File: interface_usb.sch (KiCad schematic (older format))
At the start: 5 parts

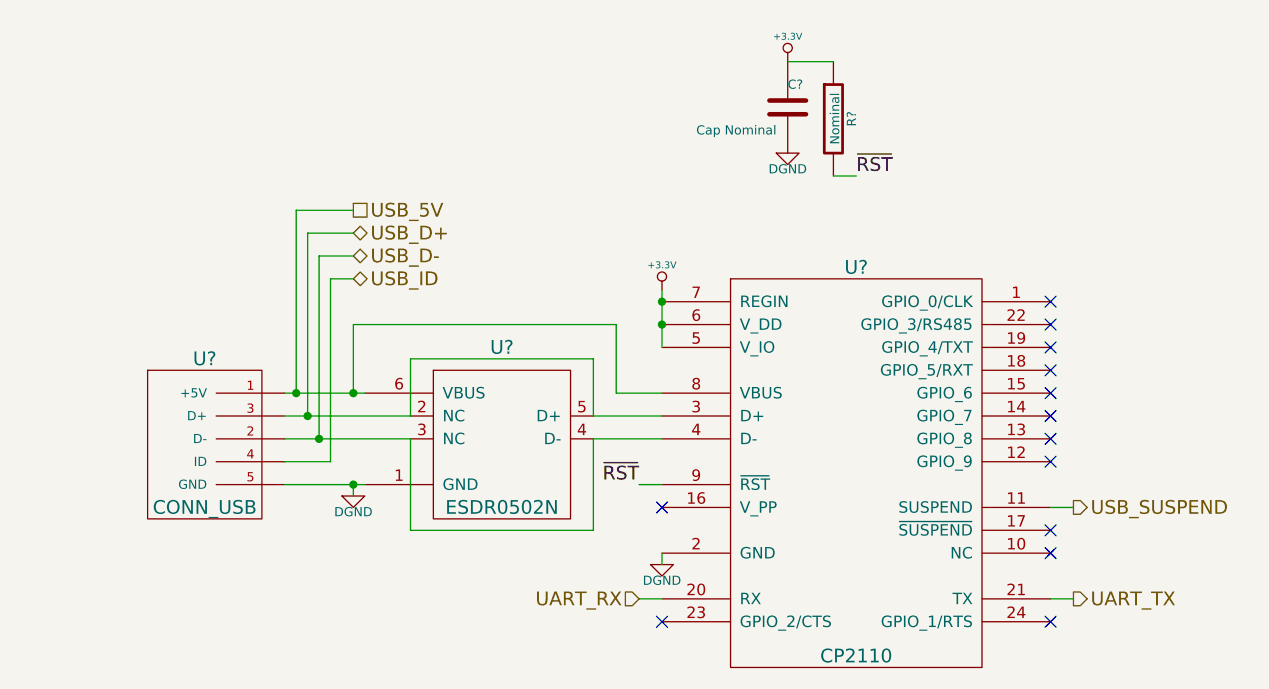
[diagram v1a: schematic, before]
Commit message: added pullups/downs as necessary, added test pts
also added interrupt conn to msp from charger, made led part for generic
indicators, added generic indicators to psu's
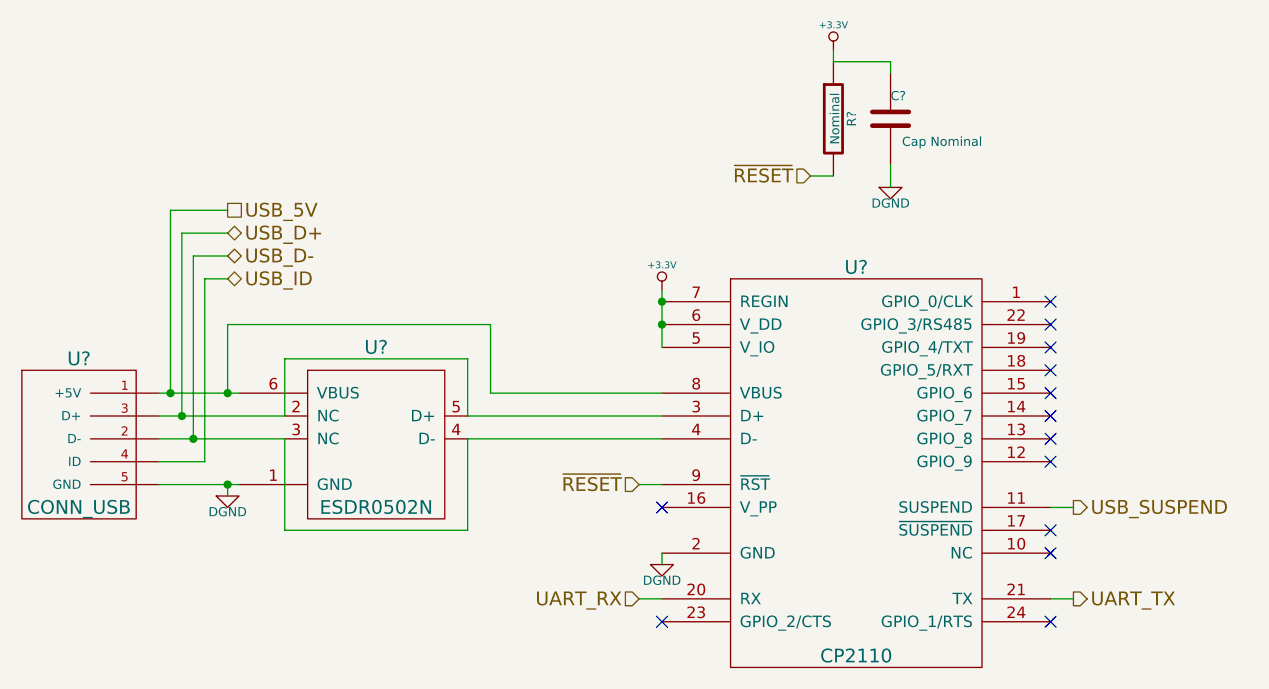
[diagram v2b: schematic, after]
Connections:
- net ~RST renamed ~RESET
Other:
- moved on the sheet: C?, U?
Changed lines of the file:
@@
 $Descr A4 11693 8268
 encoding utf-8
-Sheet 7 18
+Sheet 17 18
 Title ""
-Date "14 dec 2013"
+Date "18 dec 2013"
 Rev ""
 Comp ""
@@
 L CONN_USB U?
 U 1 1 52807223
-P 1400 2800
-F 0 "U?" H 1400 2800 60  0000 C CNN
-F 1 "CONN_USB" H 1400 2150 60  0000 C CNN
-F 2 "" H 1400 2800 60  0000 C CNN
-F 3 "" H 1400 2800 60  0000 C CNN
-	1    1400 2800
+P 850 2800
+F 0 "U?" H 850 2800 60  0000 C CNN
+F 1 "CONN_USB" H 850 2150 60  0000 C CNN
+F 2 "" H 850 2800 60  0000 C CNN
+F 3 "" H 850 2800 60  0000 C CNN
+	1    850  2800
 	1    0    0    -1
 $EndComp
@@
 L ESDR0502N U?
 U 1 1 529256B4
-P 2700 2750
-F 0 "U?" H 2700 2750 60  0000 C CNN
-F 1 "ESDR0502N" H 2700 2050 60  0000 C CNN
-F 2 "" H 2700 2750 60  0000 C CNN
-F 3 "" H 2700 2750 60  0000 C CNN
-	1    2700 2750
+P 2150 2750
+F 0 "U?" H 2150 2750 60  0000 C CNN
+F 1 "ESDR0502N" H 2150 2050 60  0000 C CNN
+F 2 "" H 2150 2750 60  0000 C CNN
+F 3 "" H 2150 2750 60  0000 C CNN
+	1    2150 2750
 	1    0    0    -1
 $EndComp
@@
 L DGND #PWR?
 U 1 1 52925A5E
-P 2050 3400
-F 0 "#PWR?" H 2050 3400 40  0001 C CNN
-F 1 "DGND" H 2050 3330 40  0000 C CNN
-F 2 "" H 2050 3400 60  0000 C CNN
-F 3 "" H 2050 3400 60  0000 C CNN
-	1    2050 3400
-	1    0    0    -1
-$EndComp
-Wire Wire Line
-	2300 3050 2300 2800
-Wire Wire Line
-	2300 2800 3100 2800
-Wire Wire Line
-	3100 2800 3100 3050
-Wire Wire Line
-	2300 3150 2300 3550
-Wire Wire Line
-	2300 3550 3100 3550
-Wire Wire Line
-	3100 3550 3100 3150
-Wire Wire Line
-	1750 2950 1800 2950
-Wire Wire Line
-	1800 2950 2050 2950
-Wire Wire Line
-	2050 2950 2100 2950
-Wire Wire Line
-	1750 3350 2050 3350
-Wire Wire Line
-	2050 3350 2100 3350
-Wire Wire Line
-	2050 3350 2050 3400
-Connection ~ 2050 3350
-Wire Wire Line
-	3100 3050 3400 3050
-Wire Wire Line
-	3100 3150 3400 3150
-Wire Wire Line
-	1750 3050 1850 3050
-Wire Wire Line
-	1850 3050 2300 3050
-Wire Wire Line
-	1750 3150 1900 3150
-Wire Wire Line
-	1900 3150 2300 3150
+P 1500 3400
+F 0 "#PWR?" H 1500 3400 40  0001 C CNN
+F 1 "DGND" H 1500 3330 40  0000 C CNN
+F 2 "" H 1500 3400 60  0000 C CNN
+F 3 "" H 1500 3400 60  0000 C CNN
+	1    1500 3400
+	1    0    0    -1
+$EndComp
+Wire Wire Line
+	1750 3050 1750 2800
+Wire Wire Line
+	1750 3150 1750 3550
+Wire Wire Line
+	1200 2950 1250 2950
+Wire Wire Line
+	1250 2950 1500 2950
+Wire Wire Line
+	1500 2950 1550 2950
+Wire Wire Line
+	1200 3350 1500 3350
+Wire Wire Line
+	1500 3350 1550 3350
+Wire Wire Line
+	1500 3350 1500 3400
+Connection ~ 1500 3350
+Wire Wire Line
+	2550 3050 3400 3050
+Wire Wire Line
+	2550 3150 3400 3150
+Wire Wire Line
+	1200 3050 1300 3050
+Wire Wire Line
+	1300 3050 1750 3050
+Wire Wire Line
+	1200 3150 1350 3150
+Wire Wire Line
+	1350 3150 1750 3150
 Wire Wire Line
 	3400 2500 3400 2550
@@
 L C C?
 U 1 1 52927D03
-P 3950 1700
-F 0 "C?" H 3950 1800 40  0000 L CNN
-F 1 "Cap Nominal" H 3550 1600 40  0000 L CNN
-F 2 "~" H 3988 1550 30  0000 C CNN
-F 3 "~" H 3950 1700 60  0000 C CNN
-	1    3950 1700
+P 4400 1750
+F 0 "C?" H 4400 1850 40  0000 L CNN
+F 1 "Cap Nominal" H 4450 1650 40  0000 L CNN
+F 2 "~" H 4438 1600 30  0000 C CNN
+F 3 "~" H 4400 1750 60  0000 C CNN
+	1    4400 1750
 	1    0    0    -1
 $EndComp
@@
 L +3.3V #PWR?
 U 1 1 52927D0F
-P 3950 1500
-F 0 "#PWR?" H 3950 1460 30  0001 C CNN
-F 1 "+3.3V" H 3950 1610 30  0000 C CNN
-F 2 "" H 3950 1500 60  0000 C CNN
-F 3 "" H 3950 1500 60  0000 C CNN
-	1    3950 1500
+P 4150 1450
+F 0 "#PWR?" H 4150 1410 30  0001 C CNN
+F 1 "+3.3V" H 4150 1560 30  0000 C CNN
+F 2 "" H 4150 1450 60  0000 C CNN
+F 3 "" H 4150 1450 60  0000 C CNN
+	1    4150 1450
 	1    0    0    -1
 $EndComp
@@
 L DGND #PWR?
 U 1 1 52927D15
-P 3950 1900
-F 0 "#PWR?" H 3950 1900 40  0001 C CNN
-F 1 "DGND" H 3950 1830 40  0000 C CNN
-F 2 "" H 3950 1900 60  0000 C CNN
-F 3 "" H 3950 1900 60  0000 C CNN
-	1    3950 1900
-	1    0    0    -1
-$EndComp
-Wire Wire Line
-	2050 2950 2050 2650
-Wire Wire Line
-	2050 2650 3200 2650
-Wire Wire Line
-	3200 2650 3200 2950
-Wire Wire Line
-	3200 2950 3400 2950
-Connection ~ 2050 2950
+P 4400 2050
+F 0 "#PWR?" H 4400 2050 40  0001 C CNN
+F 1 "DGND" H 4400 1980 40  0000 C CNN
+F 2 "" H 4400 2050 60  0000 C CNN
+F 3 "" H 4400 2050 60  0000 C CNN
+	1    4400 2050
+	1    0    0    -1
+$EndComp
+Wire Wire Line
+	1500 2950 1500 2650
+Wire Wire Line
+	1500 2650 2650 2650
+Wire Wire Line
+	2650 2650 2650 2950
+Wire Wire Line
+	2650 2950 3400 2950
+Connection ~ 1500 2950
 NoConn ~ 3400 3450
 $Comp
@@
 $EndComp
 Wire Wire Line
-	3950 1500 4150 1500
-Wire Wire Line
-	4150 2000 4250 2000
-Text Label 4250 2000 0    60   ~ 0
-~RST
-Text Label 3300 3350 2    60   ~ 0
-~RST
+	4150 1450 4150 1500
+Wire Wire Line
+	4150 2000 4050 2000
 Wire Wire Line
 	3300 3350 3400 3350
@@
 	5100 3450 5200 3450
 Wire Wire Line
-	1800 2950 1800 2150
-Wire Wire Line
-	1800 2150 2050 2150
-Connection ~ 1800 2950
-Wire Wire Line
-	1850 3050 1850 2250
-Wire Wire Line
-	1850 2250 2050 2250
-Connection ~ 1850 3050
-Wire Wire Line
-	1900 3150 1900 2350
-Wire Wire Line
-	1900 2350 2050 2350
-Connection ~ 1900 3150
-Wire Wire Line
-	1750 3250 1950 3250
-Wire Wire Line
-	1950 3250 1950 2450
-Wire Wire Line
-	1950 2450 2050 2450
-Text HLabel 2050 2150 2    60   UnSpc ~ 0
+	1250 2950 1250 2150
+Wire Wire Line
+	1250 2150 1500 2150
+Connection ~ 1250 2950
+Wire Wire Line
+	1300 3050 1300 2250
+Wire Wire Line
+	1300 2250 1500 2250
+Connection ~ 1300 3050
+Wire Wire Line
+	1350 3150 1350 2350
+Wire Wire Line
+	1350 2350 1500 2350
+Connection ~ 1350 3150
+Wire Wire Line
+	1200 3250 1400 3250
+Wire Wire Line
+	1400 3250 1400 2450
+Wire Wire Line
+	1400 2450 1500 2450
+Text HLabel 1500 2150 2    60   UnSpc ~ 0
 USB_5V
-Text HLabel 2050 2250 2    60   BiDi ~ 0
+Text HLabel 1500 2250 2    60   BiDi ~ 0
 USB_D+
-Text HLabel 2050 2350 2    60   BiDi ~ 0
+Text HLabel 1500 2350 2    60   BiDi ~ 0
 USB_D-
-Text HLabel 2050 2450 2    60   BiDi ~ 0
+Text HLabel 1500 2450 2    60   BiDi ~ 0
 USB_ID
+Wire Wire Line
+	4400 1950 4400 2050
+Wire Wire Line
+	4150 1500 4400 1500
+Wire Wire Line
+	4400 1500 4400 1550
+Text HLabel 3300 3350 0    60   Input ~ 0
+~RESET
+Wire Wire Line
+	2550 3050 2550 2800
+Wire Wire Line
+	2550 3150 2550 3550
+Wire Wire Line
+	2550 3550 1750 3550
+Wire Wire Line
+	2550 2800 1750 2800
+Text HLabel 4050 2000 0    60   Input ~ 0
+~RESET
 $EndSCHEMATC

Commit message: various fixes due to issues found in ERC
learned how to use invisible pins
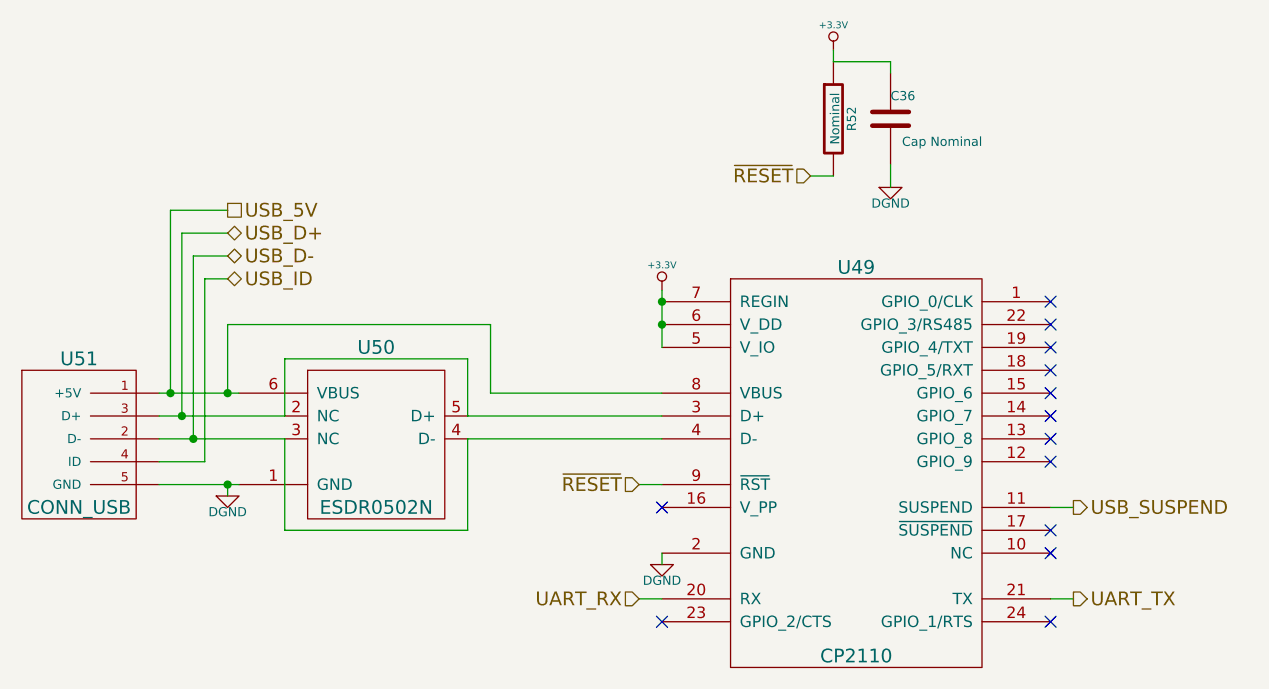
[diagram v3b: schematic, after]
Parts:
- gave numbers to parts that had none: 5
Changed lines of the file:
@@
 Sheet 17 18
 Title ""
-Date "18 dec 2013"
+Date "20 dec 2013"
 Rev ""
 Comp ""
@@
 $EndDescr
 $Comp
-L CONN_USB U?
+L CONN_USB U51
 U 1 1 52807223
 P 850 2800
-F 0 "U?" H 850 2800 60  0000 C CNN
+F 0 "U51" H 850 2800 60  0000 C CNN
 F 1 "CONN_USB" H 850 2150 60  0000 C CNN
 F 2 "" H 850 2800 60  0000 C CNN
@@
 $EndComp
 $Comp
-L CP2110 U?
+L CP2110 U49
 U 1 1 5291A63B
 P 4250 2400
-F 0 "U?" H 4250 2400 60  0000 C CNN
+F 0 "U49" H 4250 2400 60  0000 C CNN
 F 1 "CP2110" H 4250 700 60  0000 C CNN
 F 2 "" H 4250 2400 60  0000 C CNN
@@
 $EndComp
 $Comp
-L ESDR0502N U?
+L ESDR0502N U50
 U 1 1 529256B4
 P 2150 2750
-F 0 "U?" H 2150 2750 60  0000 C CNN
+F 0 "U50" H 2150 2750 60  0000 C CNN
 F 1 "ESDR0502N" H 2150 2050 60  0000 C CNN
 F 2 "" H 2150 2750 60  0000 C CNN
@@
 $EndComp
 $Comp
-L +3.3V #PWR?
+L +3.3V #PWR0115
 U 1 1 52925A58
 P 3400 2500
-F 0 "#PWR?" H 3400 2460 30  0001 C CNN
+F 0 "#PWR0115" H 3400 2460 30  0001 C CNN
 F 1 "+3.3V" H 3400 2610 30  0000 C CNN
 F 2 "" H 3400 2500 60  0000 C CNN
@@
 $EndComp
 $Comp
-L DGND #PWR?
+L DGND #PWR0116
 U 1 1 52925A5E
 P 1500 3400
-F 0 "#PWR?" H 1500 3400 40  0001 C CNN
+F 0 "#PWR0116" H 1500 3400 40  0001 C CNN
 F 1 "DGND" H 1500 3330 40  0000 C CNN
 F 2 "" H 1500 3400 60  0000 C CNN
@@
 	1750 3150 1750 3550
 Wire Wire Line
-	1200 2950 1250 2950
+	1200 2950 1550 2950
 Wire Wire Line
-	1250 2950 1500 2950
-Wire Wire Line
-	1500 2950 1550 2950
-Wire Wire Line
-	1200 3350 1500 3350
-Wire Wire Line
-	1500 3350 1550 3350
+	1200 3350 1550 3350
 Wire Wire Line
 	1500 3350 1500 3400
@@
 	2550 3150 3400 3150
 Wire Wire Line
-	1200 3050 1300 3050
+	1200 3050 1750 3050
 Wire Wire Line
-	1300 3050 1750 3050
+	1200 3150 1750 3150
 Wire Wire Line
-	1200 3150 1350 3150
-Wire Wire Line
-	1350 3150 1750 3150
-Wire Wire Line
-	3400 2500 3400 2550
-Wire Wire Line
-	3400 2550 3400 2650
-Wire Wire Line
-	3400 2650 3400 2750
+	3400 2500 3400 2750
 Connection ~ 3400 2550
 Connection ~ 3400 2650
 $Comp
-L DGND #PWR?
+L DGND #PWR0117
 U 1 1 52927CD7
 P 3400 3700
-F 0 "#PWR?" H 3400 3700 40  0001 C CNN
+F 0 "#PWR0117" H 3400 3700 40  0001 C CNN
 F 1 "DGND" H 3400 3630 40  0000 C CNN
 F 2 "" H 3400 3700 60  0000 C CNN
@@
 	3400 3650 3400 3700
 $Comp
-L C C?
+L C C36
 U 1 1 52927D03
 P 4400 1750
-F 0 "C?" H 4400 1850 40  0000 L CNN
+F 0 "C36" H 4400 1850 40  0000 L CNN
 F 1 "Cap Nominal" H 4450 1650 40  0000 L CNN
 F 2 "~" H 4438 1600 30  0000 C CNN
@@
 $EndComp
 $Comp
-L +3.3V #PWR?
+L +3.3V #PWR0118
 U 1 1 52927D0F
 P 4150 1450
-F 0 "#PWR?" H 4150 1410 30  0001 C CNN
+F 0 "#PWR0118" H 4150 1410 30  0001 C CNN
 F 1 "+3.3V" H 4150 1560 30  0000 C CNN
 F 2 "" H 4150 1450 60  0000 C CNN
@@
 $EndComp
 $Comp
-L DGND #PWR?
+L DGND #PWR0119
 U 1 1 52927D15
 P 4400 2050
-F 0 "#PWR?" H 4400 2050 40  0001 C CNN
+F 0 "#PWR0119" H 4400 2050 40  0001 C CNN
 F 1 "DGND" H 4400 1980 40  0000 C CNN
 F 2 "" H 4400 2050 60  0000 C CNN
@@
 NoConn ~ 3400 3450
 $Comp
-L R R?
+L R R52
 U 1 1 52927D44
 P 4150 1750
-F 0 "R?" V 4230 1750 40  0000 C CNN
+F 0 "R52" V 4230 1750 40  0000 C CNN
 F 1 "Nominal" V 4157 1751 40  0000 C CNN
 F 2 "~" V 4080 1750 30  0000 C CNN

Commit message: started figuring out how to get pcb going
also need to figure out how to make some footprints, although there is a
nice library of footprints avalible already
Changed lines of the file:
@@
 Sheet 17 18
 Title ""
-Date "20 dec 2013"
+Date "21 dec 2013"
 Rev ""
 Comp ""
@@
 $EndComp
 $Comp
-L +3.3V #PWR0115
+L +3.3V #PWR0117
 U 1 1 52925A58
 P 3400 2500
-F 0 "#PWR0115" H 3400 2460 30  0001 C CNN
+F 0 "#PWR0117" H 3400 2460 30  0001 C CNN
 F 1 "+3.3V" H 3400 2610 30  0000 C CNN
 F 2 "" H 3400 2500 60  0000 C CNN
@@
 $EndComp
 $Comp
-L DGND #PWR0116
+L DGND #PWR0118
 U 1 1 52925A5E
 P 1500 3400
-F 0 "#PWR0116" H 1500 3400 40  0001 C CNN
+F 0 "#PWR0118" H 1500 3400 40  0001 C CNN
 F 1 "DGND" H 1500 3330 40  0000 C CNN
 F 2 "" H 1500 3400 60  0000 C CNN
@@
 Connection ~ 3400 2650
 $Comp
-L DGND #PWR0117
+L DGND #PWR0119
 U 1 1 52927CD7
 P 3400 3700
-F 0 "#PWR0117" H 3400 3700 40  0001 C CNN
+F 0 "#PWR0119" H 3400 3700 40  0001 C CNN
 F 1 "DGND" H 3400 3630 40  0000 C CNN
 F 2 "" H 3400 3700 60  0000 C CNN
@@
 $EndComp
 $Comp
-L +3.3V #PWR0118
+L +3.3V #PWR0120
 U 1 1 52927D0F
 P 4150 1450
-F 0 "#PWR0118" H 4150 1410 30  0001 C CNN
+F 0 "#PWR0120" H 4150 1410 30  0001 C CNN
 F 1 "+3.3V" H 4150 1560 30  0000 C CNN
 F 2 "" H 4150 1450 60  0000 C CNN
@@
 $EndComp
 $Comp
-L DGND #PWR0119
+L DGND #PWR0121
 U 1 1 52927D15
 P 4400 2050
-F 0 "#PWR0119" H 4400 2050 40  0001 C CNN
+F 0 "#PWR0121" H 4400 2050 40  0001 C CNN
 F 1 "DGND" H 4400 1980 40  0000 C CNN
 F 2 "" H 4400 2050 60  0000 C CNN
@@
 	5100 3450 5200 3450
 Wire Wire Line
-	1250 2950 1250 2150
+	1250 2100 1250 2950
 Wire Wire Line
 	1250 2150 1500 2150
@@
 Text HLabel 4050 2000 0    60   Input ~ 0
 ~RESET
+$Comp
+L PWR_FLAG #FLG0122
+U 1 1 52B609A1
+P 1250 2100
+F 0 "#FLG0122" H 1250 2195 30  0001 C CNN
+F 1 "PWR_FLAG" H 1250 2280 30  0000 C CNN
+F 2 "" H 1250 2100 60  0000 C CNN
+F 3 "" H 1250 2100 60  0000 C CNN
+	1    1250 2100
+	1    0    0    -1
+$EndComp
+$Comp
+L PWR_FLAG #FLG0123
+U 1 1 52B609AE
+P 1250 3400
+F 0 "#FLG0123" H 1250 3495 30  0001 C CNN
+F 1 "PWR_FLAG" H 1250 3580 30  0000 C CNN
+F 2 "" H 1250 3400 60  0000 C CNN
+F 3 "" H 1250 3400 60  0000 C CNN
+	1    1250 3400
+	-1   0    0    1
+$EndComp
+Connection ~ 1250 2150
+Wire Wire Line
+	1250 3400 1250 3350
+Connection ~ 1250 3350
 $EndSCHEMATC

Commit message: placed components ... quite the task!
there is a lot of shit going on in this board... :D
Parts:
- renumbered C36 to C30, R52 to R47, U49 to U45, U50 to U46, U51 to U47
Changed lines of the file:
@@
 $Descr A4 11693 8268
 encoding utf-8
-Sheet 17 18
+Sheet 17 15
 Title ""
-Date "12 jan 2014"
+Date "18 jan 2014"
 Rev ""
 Comp ""
@@
 $EndDescr
 $Comp
-L CONN_USB U51
+L CONN_USB U47
 U 1 1 52807223
 P 850 2800
-F 0 "U51" H 850 2800 60  0000 C CNN
+F 0 "U47" H 850 2800 60  0000 C CNN
 F 1 "CONN_USB" H 850 2150 60  0000 C CNN
 F 2 "" H 850 2800 60  0000 C CNN
@@
 $EndComp
 $Comp
-L CP2110 U49
+L CP2110 U45
 U 1 1 5291A63B
 P 4250 2400
-F 0 "U49" H 4250 2400 60  0000 C CNN
+F 0 "U45" H 4250 2400 60  0000 C CNN
 F 1 "CP2110" H 4250 700 60  0000 C CNN
 F 2 "" H 4250 2400 60  0000 C CNN
@@
 $EndComp
 $Comp
-L ESDR0502N U50
+L ESDR0502N U46
 U 1 1 529256B4
 P 2150 2750
-F 0 "U50" H 2150 2750 60  0000 C CNN
+F 0 "U46" H 2150 2750 60  0000 C CNN
 F 1 "ESDR0502N" H 2150 2050 60  0000 C CNN
 F 2 "" H 2150 2750 60  0000 C CNN
@@
 $EndComp
 $Comp
-L +3.3V #PWR0117
+L +3.3V #PWR0103
 U 1 1 52925A58
 P 3400 2500
-F 0 "#PWR0117" H 3400 2460 30  0001 C CNN
+F 0 "#PWR0103" H 3400 2460 30  0001 C CNN
 F 1 "+3.3V" H 3400 2610 30  0000 C CNN
 F 2 "" H 3400 2500 60  0000 C CNN
@@
 $EndComp
 $Comp
-L DGND #PWR0118
+L DGND #PWR0104
 U 1 1 52925A5E
 P 1500 3400
-F 0 "#PWR0118" H 1500 3400 40  0001 C CNN
+F 0 "#PWR0104" H 1500 3400 40  0001 C CNN
 F 1 "DGND" H 1500 3330 40  0000 C CNN
 F 2 "" H 1500 3400 60  0000 C CNN
@@
 Connection ~ 3400 2650
 $Comp
-L DGND #PWR0119
+L DGND #PWR0105
 U 1 1 52927CD7
 P 3400 3700
-F 0 "#PWR0119" H 3400 3700 40  0001 C CNN
+F 0 "#PWR0105" H 3400 3700 40  0001 C CNN
 F 1 "DGND" H 3400 3630 40  0000 C CNN
 F 2 "" H 3400 3700 60  0000 C CNN
@@
 	3400 3650 3400 3700
 $Comp
-L C C36
+L C C30
 U 1 1 52927D03
 P 4400 1750
-F 0 "C36" H 4400 1850 40  0000 L CNN
+F 0 "C30" H 4400 1850 40  0000 L CNN
 F 1 "Cap Nominal" H 4450 1650 40  0000 L CNN
 F 2 "~" H 4438 1600 30  0000 C CNN
@@
 $EndComp
 $Comp
-L +3.3V #PWR0120
+L +3.3V #PWR0106
 U 1 1 52927D0F
 P 4150 1450
-F 0 "#PWR0120" H 4150 1410 30  0001 C CNN
+F 0 "#PWR0106" H 4150 1410 30  0001 C CNN
 F 1 "+3.3V" H 4150 1560 30  0000 C CNN
 F 2 "" H 4150 1450 60  0000 C CNN
@@
 $EndComp
 $Comp
-L DGND #PWR0121
+L DGND #PWR0107
 U 1 1 52927D15
 P 4400 2050
-F 0 "#PWR0121" H 4400 2050 40  0001 C CNN
+F 0 "#PWR0107" H 4400 2050 40  0001 C CNN
 F 1 "DGND" H 4400 1980 40  0000 C CNN
 F 2 "" H 4400 2050 60  0000 C CNN
@@
 NoConn ~ 3400 3450
 $Comp
-L R R52
+L R R47
 U 1 1 52927D44
 P 4150 1750
-F 0 "R52" V 4230 1750 40  0000 C CNN
+F 0 "R47" V 4230 1750 40  0000 C CNN
 F 1 "Nominal" V 4157 1751 40  0000 C CNN
 F 2 "~" V 4080 1750 30  0000 C CNN
@@
 ~RESET
 $Comp
-L PWR_FLAG #FLG0122
+L PWR_FLAG #FLG0108
 U 1 1 52B609A1
 P 1250 2100
-F 0 "#FLG0122" H 1250 2195 30  0001 C CNN
+F 0 "#FLG0108" H 1250 2195 30  0001 C CNN
 F 1 "PWR_FLAG" H 1250 2280 30  0000 C CNN
 F 2 "" H 1250 2100 60  0000 C CNN
@@
 $EndComp
 $Comp
-L PWR_FLAG #FLG0123
+L PWR_FLAG #FLG0109
 U 1 1 52B609AE
 P 1250 3400
-F 0 "#FLG0123" H 1250 3495 30  0001 C CNN
+F 0 "#FLG0109" H 1250 3495 30  0001 C CNN
 F 1 "PWR_FLAG" H 1250 3580 30  0000 C CNN
 F 2 "" H 1250 3400 60  0000 C CNN
